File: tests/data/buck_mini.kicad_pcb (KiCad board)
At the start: 4 copper layers, 30 x 20 mm, 2 parts, among them Q1 HS_FET

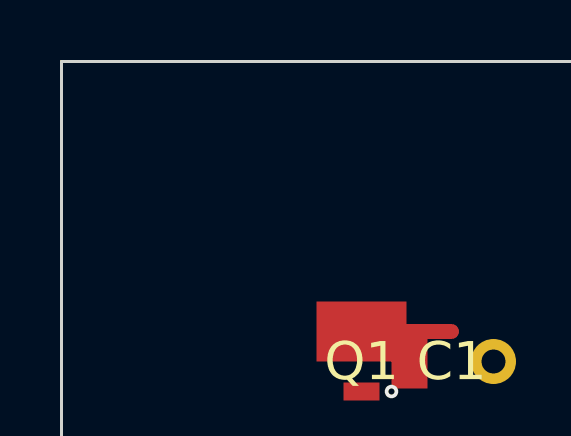
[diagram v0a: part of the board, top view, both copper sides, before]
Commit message: Stage A canonical IR, KiCad->IR converter, Stage C heterogeneous graph builder; parser keeps ids, locked flags, arcs, courtyards; package layout and architecture doc
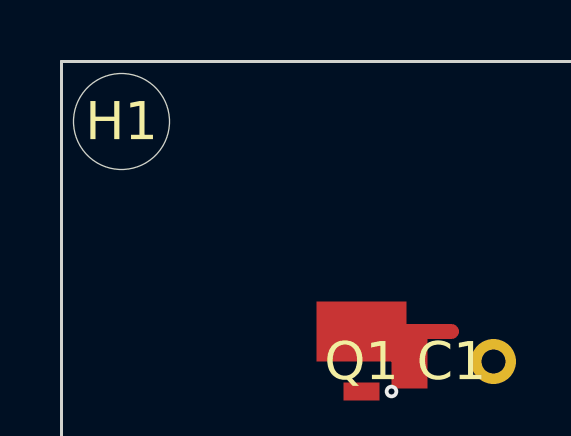
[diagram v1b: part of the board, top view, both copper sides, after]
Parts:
- added H1: MountingHole, MountingHole:MountingHole_3.2mm, F.Cu at (92.0, 92.0)
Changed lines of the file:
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@@
 		(pad "1" smd rect (at -1 0 90) (size 0.6 1.2) (layers "F.Cu" "F.Paste" "F.Mask") (net 2 "SW"))
 		(pad "5" smd rect (at 1 0 90) (size 2 3) (layers "F.Cu" "F.Paste" "F.Mask") (net 1 "VIN"))
+		(fp_rect (start -2 -1.5) (end 2 1.5) (stroke (width 0.05) (type default)) (fill none) (layer "F.CrtYd") (uuid "cy1"))
+		(uuid "fp-q1")
+	)
+	(footprint "MountingHole:MountingHole_3.2mm" (layer "F.Cu") (at 92 92) (locked yes)
+		(property "Reference" "H1" (at 0 0 0) (layer "F.SilkS"))
+		(property "Value" "MountingHole" (at 0 0 0) (layer "F.Fab"))
+		(pad "" np_thru_hole circle (at 0 0) (size 3.2 3.2) (drill 3.2) (layers "*.Cu" "*.Mask"))
 	)
 	(footprint "Capacitor_SMD:C_1206"
@@
 	)
 	(segment (start 100 99) (end 103 99) (width 0.5) (layer "F.Cu") (net 1) (uuid "s1"))
-	(via (at 101 101) (size 0.45) (drill 0.2) (layers "F.Cu" "In1.Cu") (net 3) (uuid "v1"))
+	(via (at 101 101) (size 0.45) (drill 0.2) (layers "F.Cu" "In1.Cu") (net 3) (locked yes) (uuid "v1"))
 	(arc (start 110 100) (mid 109.41421356 98.58578644) (end 108 98) (width 0.3) (layer "F.Cu") (net 2))
 	(zone (net 3) (net_name "GND") (layer "In1.Cu") (uuid "z1")
